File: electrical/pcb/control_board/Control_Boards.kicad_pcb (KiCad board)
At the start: 2 copper layers, 181.6 x 252.8 mm, 138 parts, among them J1 XT30-M, J10 Molex_172675-0613, J11 Molex_172675-0613, J12 TSW-104-07-F-T, J13 Molex_172675-0613, J14 Molex_172675-0613, J15 TSW-104-07-F-T, J16 277-11404-ND, J17 277-11404-ND, J18 277-11404-ND, J19 TSW-104-07-F-T, J2 XT30-F, J20 PEC08SAAN, J21 PPTC102LFBN-RC, J22 S9175-ND_rpi_breakout, J23 S9175-ND_rpi_breakout, J24 6posheader, J25 SSW-104-01-F-T, J26 WM6548-ND, J27 PPTC021LFBN-RC, J28 PPTC021LFBN-RC, J29 PPTC021LFBN-RC, J3 XT30-F, J30 PEC08SAAN, J4 XT30-F, J5 XT30-M, J6 ED2580-ND, J7 TSW-104-07-F-T, J8 Molex_172675-0613, J9 Molex_172675-0613, M1 Mounting_Holes, Q1 2N3906, Q2 2N3906, Q3 2N3906, SW1 CT206124-ND, T1 test_point, T10 test_point, T11 test_point, T12 test_point, T13 test_point, T14 test_point, T15 test_point, T2 test_point, T3 test_point, T4 test_point, T5 test_point, T6 test_point, T7 test_point, T8 test_point, T9 test_point, U1 INA260, U2 PCA9685, U3 D24V22Fx, U4 D24V150Fx, U5 DC7G3HWA, U6 DC7G3HWA, y1 rover_silkscreen

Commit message: progress on new boards layout
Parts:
- removed ? (x4): , 
- removed C31: 100nf, Resistor_THT:R_Axial_DIN0207_L6.3mm_D2.5mm_P7.62mm_Horizontal
- removed D7: 1N4148, Diode_THT:D_DO-35_SOD27_P7.62mm_Horizontal
- removed the T1 at (72.4, -111.1)
- removed the T2 at (14.6, -138.4)
- removed the T3 at (118.7, -128.3)
- removed the T4 at (144.1, -134.0)
- removed the T5 at (72.4, -115.6)
- added C7: 10uf, Capacitor_THT:CP_Radial_D8.0mm_P3.80mm, F.Cu at (626.8, -59.1)
- added Q4: 2N3906, Package_TO_SOT_THT:TO-92_Inline, F.Cu at (543.1, -46.4)
- added Q5: 2N3906, Package_TO_SOT_THT:TO-92_Inline, F.Cu at (541.5, -31.5)
- added Q6: 2N3906, Package_TO_SOT_THT:TO-92_Inline, F.Cu at (542.1, -17.2)
- added R29: 82, Resistor_THT:R_Axial_DIN0207_L6.3mm_D2.5mm_P7.62mm_Horizontal, F.Cu at (582.9, -84.3)
- added R30: 0, Resistor_THT:R_Axial_DIN0207_L6.3mm_D2.5mm_P7.62mm_Horizontal, F.Cu at (551.1, -84.4)
- added R31: 4.7k, Resistor_THT:R_Axial_DIN0207_L6.3mm_D2.5mm_P7.62mm_Horizontal, F.Cu at (618.2, -24.5)
- added R32: 4.7k, Resistor_THT:R_Axial_DIN0207_L6.3mm_D2.5mm_P7.62mm_Horizontal, F.Cu at (593.6, -34.3)
- added R33: 4.7k, Resistor_THT:R_Axial_DIN0207_L6.3mm_D2.5mm_P7.62mm_Horizontal, F.Cu at (593.9, -29.7)
- added R34: 4.7k, Resistor_THT:R_Axial_DIN0207_L6.3mm_D2.5mm_P7.62mm_Horizontal, F.Cu at (594.2, -25.5)
- added R35: 4.7k, Resistor_THT:R_Axial_DIN0207_L6.3mm_D2.5mm_P7.62mm_Horizontal, F.Cu at (594.2, -21.3)
- added R36: 10k, Resistor_THT:R_Axial_DIN0207_L6.3mm_D2.5mm_P7.62mm_Horizontal, F.Cu at (561.9, -46.4)
- added R37: 10k, Resistor_THT:R_Axial_DIN0207_L6.3mm_D2.5mm_P7.62mm_Horizontal, F.Cu at (560.6, -31.4)
- added R38: 10k, Resistor_THT:R_Axial_DIN0207_L6.3mm_D2.5mm_P7.62mm_Horizontal, F.Cu at (561.8, -17.4)
- added U7: MIC2937A-3.3WT, Package_TO_SOT_THT:TO-220-3_Vertical, F.Cu at (627.0, -67.4)
- C25, C27, C28: footprint Resistor_THT:R_Axial_DIN0207_L6.3mm_D2.5mm_P7.62mm_Horizontal -> Capacitor_THT:CP_Radial_D8.0mm_P3.80mm
- Q1, R11, R15: moved to F.Cu
- R1: value 10k -> 1k
- R18: value 200 -> 68
- R19, R20: value 200 -> 68; moved to F.Cu
- R22, R23, R24: value 82 -> 68
- R6, R7: value 680 -> 1k
- R8: value 470 -> 680
- R9: value 150 -> 220
- moved R11 557.4 mm to (617.6, -29.6), turned to 0 degrees
- moved R20 538.4 mm to (550.8, -17.5), turned to 0 degrees
- moved R19 536.1 mm to (550.3, -31.6), turned to 0 degrees
- moved R24 525.2 mm to (562.2, -63.1)
- moved R12 520.1 mm to (516.4, -59.9), turned to 0 degrees
- moved R13 517.7 mm to (517.0, -55.5), turned to 0 degrees
- moved R14 514.7 mm to (517.3, -51.0), turned to 0 degrees
- moved R15 498.4 mm to (551.8, -63.3), turned to 0 degrees
- moved Q1 492.2 mm to (544.0, -63.3), turned to 0 degrees
- moved T15 322.3 mm to (546.9, 32.9)
- moved T13 322.3 mm to (541.9, 32.9)
- moved T14 322.3 mm to (544.4, 32.9)
- moved T5 315.6 mm to (562.6, 17.5)
- moved C25 311.0 mm to (385.6, 6.79)
- moved C27 311.0 mm to (393.3, -21.1)
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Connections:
- net /Brain Board/X_RPI_GPIO_GEN0 renamed /Brain Board/RPI_LED_5
- J22 pad 1: +3.3V_brain -> /Brain Board/3.3V_rpi
- J22 pad 16: /Brain Board/E_STOP_pi -> /Brain Board/ESTOP_in_1_pi
- J22 pad 17: +3.3V_brain -> /Brain Board/3.3V_rpi
- J23 pad 1: +3.3V_brain -> /Brain Board/3.3V_rpi
- J23 pad 16: /Brain Board/E_STOP_pi -> /Brain Board/ESTOP_in_1_pi
- J23 pad 17: +3.3V_brain -> /Brain Board/3.3V_rpi
- J27 pad 1: /Brain Board/E_STOP2_in -> /Brain Board/ESTOP_in_2
- J28 pad 1: /Brain Board/E_STOP3_in -> /Brain Board/ESTOP_in_3
- Q1 pad 1: +3.3V_brain -> +3.3V_motor
- R11 pad 1: +5V_brain -> /Brain Board/RXD
- R11 pad 2: /Brain Board/RXD -> +5V_motor
- R12 pad 1: /Brain Board/E_STOP_pi -> /Motor Board/E_STOP
- R12 pad 2: GND_brain -> GND_motor
- R13 pad 1: /Brain Board/E_STOP2_in -> /Motor Board/E_STOP2
- R13 pad 2: GND_brain -> GND_motor
- R14 pad 1: /Brain Board/E_STOP3_in -> /Motor Board/E_STOP3
- R14 pad 2: GND_brain -> GND_motor
- R15 pad 2: Net-(D7-Pad2) -> /Motor Board/alert
- R18 pad 2: /Brain Board/E_STOP -> Net-(Q4-Pad3)
- R19 pad 2: /Brain Board/E_STOP2 -> Net-(Q5-Pad3)
- R20 pad 2: /Brain Board/E_STOP3 -> Net-(Q6-Pad3)
- R24 pad 1: /Brain Board/ALERT_LED -> /Motor Board/ALERT_LED
- R25 pad 1: Net-(R25-Pad1) -> /Brain Board/RPI_LED_1
- R25 pad 2: /Brain Board/RPI_LED_1 -> Net-(R25-Pad2)
- R26 pad 1: Net-(R26-Pad1) -> /Brain Board/RPI_LED_2
- R26 pad 2: /Brain Board/RPI_LED_2 -> Net-(R26-Pad2)
- R27 pad 1: Net-(R27-Pad1) -> /Brain Board/RPI_LED_3
- R27 pad 2: /Brain Board/RPI_LED_3 -> Net-(R27-Pad2)
- R28 pad 1: Net-(R28-Pad1) -> /Brain Board/RPI_LED_4
- R28 pad 2: /Brain Board/RPI_LED_4 -> Net-(R28-Pad2)
- SW1 pad 10: +5V_brain -> /Brain Board/ESTOP_in_3
- SW1 pad 12: /Brain Board/E_STOP3_in -> +3.3V_brain
- SW1 pad 2: +5V_brain -> /Brain Board/ESTOP_in_1_pi
- SW1 pad 4: /Brain Board/E_STOP_pi -> +3.3V_brain
- SW1 pad 6: +5V_brain -> /Brain Board/ESTOP_in_2
- SW1 pad 8: /Brain Board/E_STOP2_in -> +3.3V_brain
- U5 pad 10: Net-(U5-Pad10) -> /Motor Board/ALERT_LED
- U6 pad 10: /Brain Board/ESTOP_LED_1 -> /Brain Board/ESTOP_LED_3
- U6 pad 13: GND_brain -> Net-(R25-Pad2)
- U6 pad 14: GND_brain -> Net-(R26-Pad2)
- U6 pad 15: GND_brain -> Net-(R27-Pad2)
- U6 pad 16: GND_brain -> Net-(R28-Pad2)
- U6 pad 17: GND_brain -> Net-(R29-Pad2)
- U6 pad 3: /Brain Board/ALERT_LED -> +3.3V_brain
- U6 pad 4: Net-(R25-Pad1) -> +3.3V_brain
- U6 pad 5: Net-(R26-Pad1) -> +3.3V_brain
- U6 pad 6: Net-(R27-Pad1) -> +3.3V_brain
- U6 pad 7: Net-(R28-Pad1) -> +3.3V_brain
- U6 pad 8: /Brain Board/ESTOP_LED_3 -> /Brain Board/ESTOP_LED_1
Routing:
- net /Motor Board/RXD: track 394.1 -> 0.00 mm, vias 15 -> 0
- net /Motor Board/SDA_rpi: track 392.1 -> 0.00 mm, vias 18 -> 0
- net /Motor Board/SCL_rpi: track 386.0 -> 0.00 mm, vias 18 -> 0
- net /Motor Board/E_STOP: track 348.8 -> 0.00 mm, vias 8 -> 0
- net /Motor Board/TXD: track 344.3 -> 0.00 mm, vias 20 -> 0
- net /Motor Board/E_STOP2: track 338.3 -> 0.00 mm, vias 9 -> 0
- net /Motor Board/E_STOP3: track 333.2 -> 0.00 mm, vias 10 -> 0
- net +5V_brain: track 311.5 -> 0.00 mm, vias 7 -> 0
- net +3.3V_motor: track 262.8 -> 0.00 mm, vias 9 -> 0
- net /Motor Board/RC2EN1B: track 252.3 -> 0.00 mm, vias 14 -> 0
- net /Motor Board/RC2EN1A: track 250.5 -> 0.00 mm, vias 13 -> 0
- net /Motor Board/RC2EN2B: track 249.2 -> 0.00 mm, vias 15 -> 0
- net +3.3V_brain: track 247.3 -> 0.00 mm, vias 2 -> 0
- net /Motor Board/RC2EN2A: track 229.3 -> 0.00 mm, vias 13 -> 0
- net /Motor Board/RC1EN2A: track 201.1 -> 0.00 mm, vias 9 -> 0
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- removed copper zone on B.Cu, net +12V_motor
- removed copper zone on F.Cu, net +5V_motor
- removed copper zone on F.Cu, net +BATT
- removed copper zone on B.Cu, net /Motor Board/BATTNEG
- removed copper zone on F.Cu, net /Motor Board/BATTPOS
- removed copper zone on B.Cu, net /Motor Board/MMLOAD+
- removed copper zone on F.Cu, net /Motor Board/SWITCH+
- removed copper zone on F.Cu, net /Motor Board/SWITCH-
- removed copper zone on B.Cu, net GND_brain
- removed copper zone on B.Cu, net GND_motor
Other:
- board size 181.6 x 252.8 mm -> 220 x 367.6 mm

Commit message: rough draft layout v1 for motor board
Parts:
- C3, C7, Q1, R15, R21, R24, R30, U1, U2, U3, U7: moved to B.Cu
- J2: value XT30-F -> ED2580-ND; footprint JPL Robotics:AMASS_XT30U-F_1x02_P5.0mm_Vertical -> JPL Robotics:ED2580-ND
- moved U7 595.4 mm to (44.9, 58.1), turned to 180 degrees
- moved C7 582.8 mm to (56.2, 59.4), turned to 90 degrees
- moved T12 525.4 mm to (5.79, 37.5)
- moved T11 522.0 mm to (5.79, 32.7)
- moved T10 518.7 mm to (5.79, 27.8)
- moved T9 515.1 mm to (5.79, 23.0)
- moved T8 513.1 mm to (5.79, 18.2)
- moved T7 507.1 mm to (5.79, 13.4)
- moved R24 500.9 mm to (74.9, 52.8)
- moved R13 493.0 mm to (58.2, 124.9)
- moved R12 492.9 mm to (58.2, 121.7)
- moved R14 492.9 mm to (58.2, 128.2)
- moved R30 472.8 mm to (91.6, 26.8), turned to 270 degrees
- moved R15 471.5 mm to (94.8, 52.8)
- moved Q1 471.3 mm to (87.2, 52.7)
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
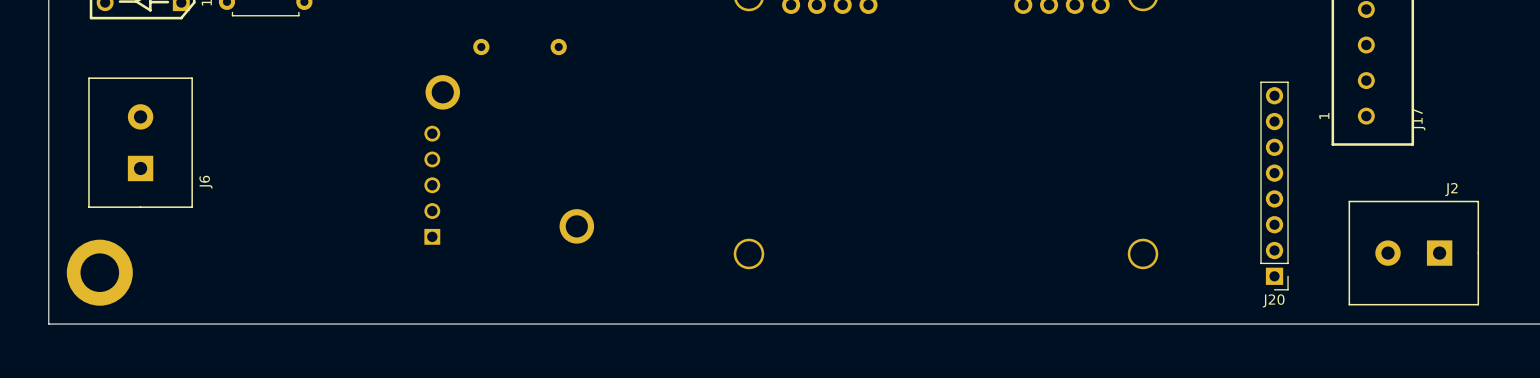
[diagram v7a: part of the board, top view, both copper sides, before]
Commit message: Updating 3d model links again, and adding arduino connector 3d model
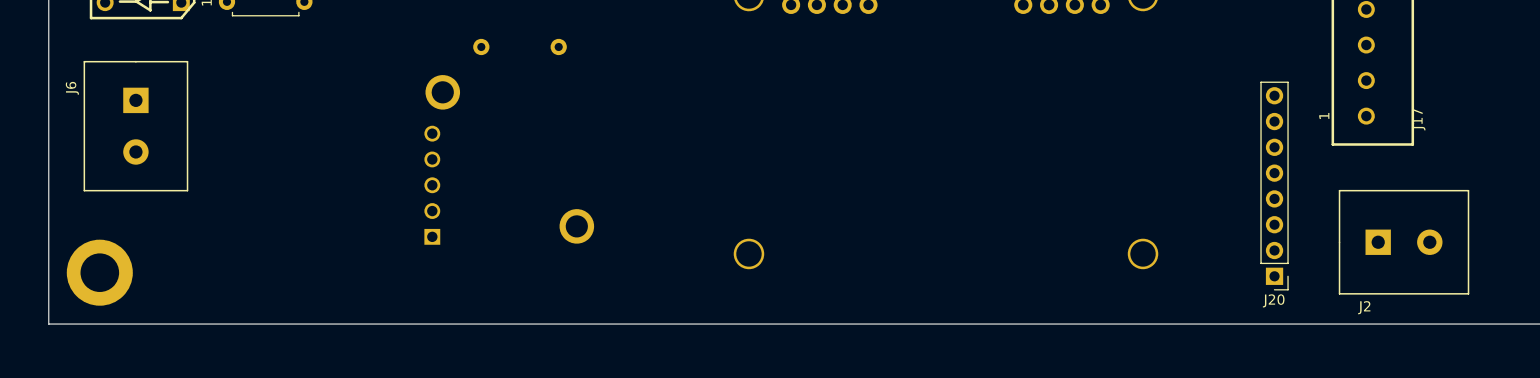
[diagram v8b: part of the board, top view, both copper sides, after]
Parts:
- moved J6 6.72 mm to (8.59, 78.0), turned to 270 degrees
- moved J2 6.14 mm to (130.9, 91.9), turned to 0 degrees
